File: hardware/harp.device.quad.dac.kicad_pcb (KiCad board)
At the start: 4 copper layers, 123 x 60 mm, 394 parts, among them J1 Conn_01x04_Pin, J10 USB_C_Receptacle_USB2.0, J11 Conn_Coaxial, J12 Conn_Coaxial, J13 Conn_Coaxial, J14 Conn_Coaxial, J15 Conn_Coaxial, J16 Conn_Coaxial, J17 Conn_Coaxial, J18 Conn_Coaxial, J2 Conn_01x03_Male, J3 USB_C_Receptacle_USB2.0, J4 AudioJack3, J5 Conn_Coaxial, J6 Conn_Coaxial, J7 Conn_Coaxial, J8 Conn_Coaxial, J9 Barrel_Jack_Switch, U1 RP2350B-QFN80, U10 LT1678CS8#PBF, U11 LT1678CS8#PBF, U12 LT1678CS8#PBF, U13 LT1678CS8#PBF, U14 LT1461CIS8-2.5#PBF, U15 LT1678CS8#PBF, U16 LT1678CS8#PBF, U17 LM211DRG4, U18 LM211DRG4, U19 LM211DRG4, U2 LM4040A30IDBZR, U20 LM211DRG4, U21 TXB0102DCT, U22 ADUM4160, U23 74LVCH2T45DC, U24 74LVCH2T45DC, U25 74LVCH2T45DC, U26 LTC3122HMSE#PBF, U27 LTC3115IDHD-2#WPBF, U28 NCP1117-3.3_SOT223, U29 NCP1117-12_SOT223, U3 W25Q128JVS, U30 LM2990SX-12, U31 74LVCH2T45DC, U32 74LVCH2T45DC, U4 W25Q128JVS, U5 W25Q128JVS, U6 LTC2642ACDD-16#PBF, U7 LTC2642ACDD-16#PBF, U8 LTC2642ACDD-16#PBF, U9 LTC2642ACDD-16#PBF

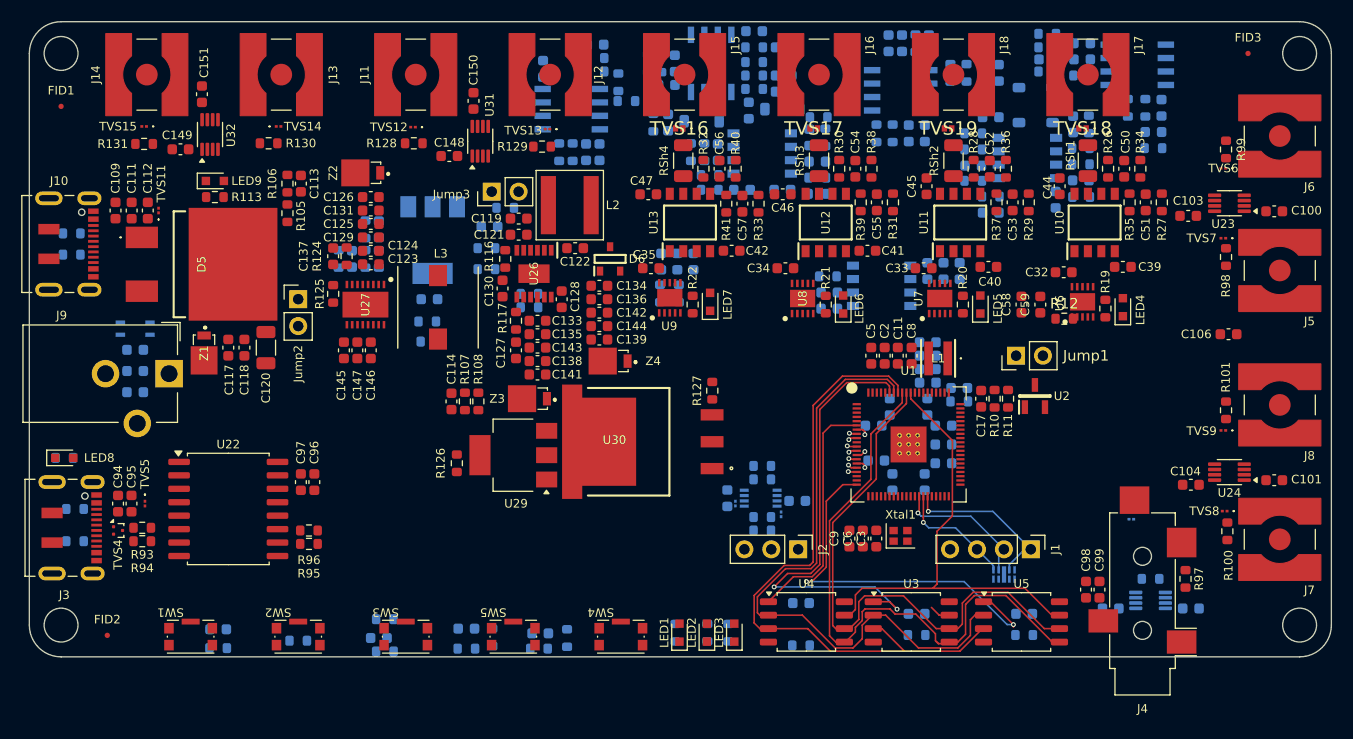
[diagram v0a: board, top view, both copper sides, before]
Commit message: Rename Some nets
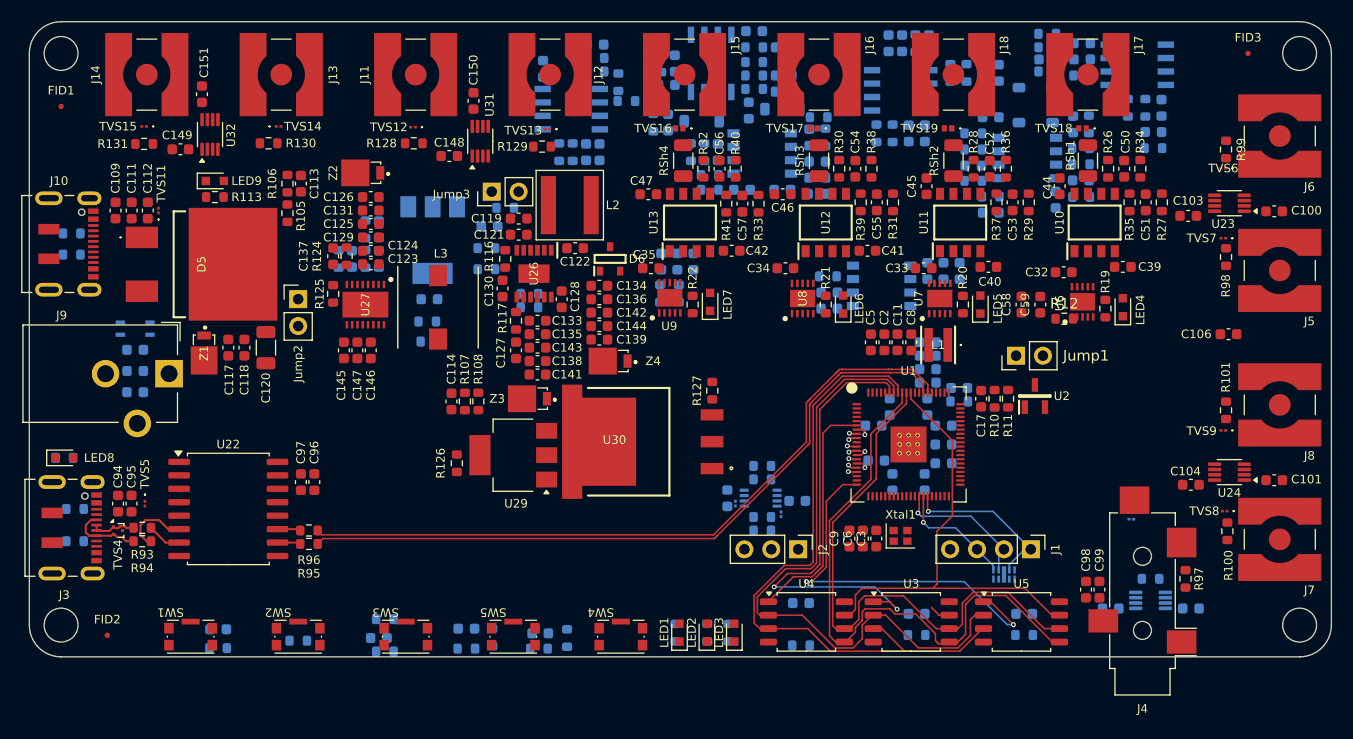
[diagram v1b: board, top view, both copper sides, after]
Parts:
- moved C5 1.27 mm to (215.4, 70.3)
- moved C8 1.27 mm to (219.2, 70.3)
- moved C11 1.27 mm to (217.9, 70.3)
- moved C2 1.27 mm to (216.6, 70.3)
- moved L1 1.27 mm to (221.7, 70.5)
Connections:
- net /Communication/PC_USB_DM renamed /Communication/PC_USB-
- net /Communication/PC_USB_DP renamed /Communication/PC_USB+
- net MC_USB_DM renamed MC_USB-
- net MC_USB_DP renamed MC_USB+
- net Net-(U22-DD+) renamed /Communication/DD+
- net Net-(U22-DD-) renamed /Communication/DD-
- net Net-(U22-UD+) renamed /Communication/UD+
- net Net-(U22-UD-) renamed /Communication/UD-
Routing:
- net MC_USB-: track 0.00 -> 67.8 mm
- net MC_USB+: track 0.00 -> 67.3 mm
- net /Communication/PC_USB-: track 0.00 -> 6.89 mm
- net /Communication/UD-: track 0.00 -> 6.37 mm
- net /Communication/PC_USB+: track 0.00 -> 4.37 mm
- net /Communication/UD+: track 0.00 -> 3.23 mm
- net /Communication/DD-: track 0.00 -> 2.20 mm
- net /Communication/DD+: track 0.00 -> 2.20 mm
